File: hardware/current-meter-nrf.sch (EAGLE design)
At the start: 47 parts, among them IC1 TINY24/44/84-SSU, IC2 LM358, IC3 MAX1555, U2 NRF24L01SMD, U3 USB-MINIB-5PIN, X1 MC2, Y1 16M

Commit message: hw: cosmetic refactor
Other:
- note added: "Radio"
- note added: "nRF"
- note removed: "nRF Radio"
- moved on the sheet: BOX1, C10, C11, C12, C13, C14, C15, C16, C17, C18, C19, C3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

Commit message: hw: nrf: progress save
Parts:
- removed R1, R2: 68, rcl:R-EU_R0603
- removed R3: 1k5, rcl:R-EU_R0603
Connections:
- removed net N$1: R2.1, R3.1, U3.D-
- removed net N$2: R1.1, U3.D+
- removed net USB_DN: IC1.(PCINT9/XTAL2)PB1, R2.2
- removed net USB_DP: IC1.(PCINT10/INT0/OC0A/CKOUT)PB2, R1.2
- new net LED: IC1.(PCINT8/XTAL1/CLKI)PB0, LED1.A
- net A_EN: now also IC1.(PCINT9/XTAL2)PB1; no longer IC1.(PCINT8/XTAL1/CLKI)PB0, LED1.A
- net VCC: no longer R3.2
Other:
- moved on the sheet: IC3, ISP1, LED1, LED2, R10, R13, TP1, TP2

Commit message: hw: nrf: progress save
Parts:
- removed LED2: (no value), led:LEDSML0805
- removed R10: 330, rcl:R-EU_R0603
- added C1, C2: 1u, rcl:C-EUC0805
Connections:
- removed net N$20: LED2.C, R10.2
- net +5V: now also C2.1
- net CHG: now also IC1.(PCINT7/ICP/OC0B/ADC7)PA7; no longer R10.1
- net GND: now also C1.2, C2.2, LED1.C; no longer R13.1
- net LED: now also R13.2; no longer LED1.A
- net N$3: now also LED1.A, R13.1; no longer LED1.C, R13.2
- net RF_IRQ: now also IC1.(PCINT10/INT0/OC0A/CKOUT)PB2; no longer IC1.(PCINT7/ICP/OC0B/ADC7)PA7
- net VCC: now also C1.1; no longer LED2.A
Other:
- moved on the sheet: IC3, LED1, R13, TP1, TP2

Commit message: hw: nrf: progress save
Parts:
- TP1, TP2: value TPTP11R -> TPTP12R; device testpad:TPTP11R -> testpad:TPTP12R
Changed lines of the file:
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@@
 <grid distance="0.1" unitdist="inch" unit="inch" style="lines" multiple="1" display="no" altdistance="0.01" altunitdist="inch" altunit="inch"/>
 <layers>
-<layer number="1" name="Top" color="4" fill="1" visible="no" active="no"/>
-<layer number="16" name="Bottom" color="1" fill="1" visible="no" active="no"/>
-<layer number="17" name="Pads" color="2" fill="1" visible="no" active="no"/>
-<layer number="18" name="Vias" color="2" fill="1" visible="no" active="no"/>
-<layer number="19" name="Unrouted" color="6" fill="1" visible="no" active="no"/>
-<layer number="20" name="Dimension" color="15" fill="1" visible="no" active="no"/>
-<layer number="21" name="tPlace" color="7" fill="1" visible="no" active="no"/>
-<layer number="22" name="bPlace" color="7" fill="1" visible="no" active="no"/>
-<layer number="23" name="tOrigins" color="15" fill="1" visible="no" active="no"/>
-<layer number="24" name="bOrigins" color="15" fill="1" visible="no" active="no"/>
-<layer number="25" name="tNames" color="7" fill="1" visible="no" active="no"/>
-<layer number="26" name="bNames" color="7" fill="1" visible="no" active="no"/>
-<layer number="27" name="tValues" color="7" fill="1" visible="no" active="no"/>
-<layer number="28" name="bValues" color="7" fill="1" visible="no" active="no"/>
+<layer number="1" name="Top" color="4" fill="1" visible="yes" active="no"/>
+<layer number="16" name="Bottom" color="1" fill="1" visible="yes" active="no"/>
+<layer number="17" name="Pads" color="2" fill="1" visible="yes" active="no"/>
+<layer number="18" name="Vias" color="2" fill="1" visible="yes" active="no"/>
+<layer number="19" name="Unrouted" color="6" fill="1" visible="yes" active="no"/>
+<layer number="20" name="Dimension" color="15" fill="1" visible="yes" active="no"/>
+<layer number="21" name="tPlace" color="7" fill="1" visible="yes" active="no"/>
+<layer number="22" name="bPlace" color="7" fill="1" visible="yes" active="no"/>
+<layer number="23" name="tOrigins" color="15" fill="1" visible="yes" active="no"/>
+<layer number="24" name="bOrigins" color="15" fill="1" visible="yes" active="no"/>
+<layer number="25" name="tNames" color="7" fill="1" visible="yes" active="no"/>
+<layer number="26" name="bNames" color="7" fill="1" visible="yes" active="no"/>
+<layer number="27" name="tValues" color="7" fill="1" visible="yes" active="no"/>
+<layer number="28" name="bValues" color="7" fill="1" visible="yes" active="no"/>
 <layer number="29" name="tStop" color="7" fill="3" visible="no" active="no"/>
 <layer number="30" name="bStop" color="7" fill="6" visible="no" active="no"/>
@@
 <layer number="35" name="tGlue" color="7" fill="4" visible="no" active="no"/>
 <layer number="36" name="bGlue" color="7" fill="5" visible="no" active="no"/>
-<layer number="37" name="tTest" color="7" fill="1" visible="no" active="no"/>
-<layer number="38" name="bTest" color="7" fill="1" visible="no" active="no"/>
+<layer number="37" name="tTest" color="7" fill="1" visible="yes" active="no"/>
+<layer number="38" name="bTest" color="7" fill="1" visible="yes" active="no"/>
 <layer number="39" name="tKeepout" color="4" fill="11" visible="no" active="no"/>
 <layer number="40" name="bKeepout" color="1" fill="11" visible="no" active="no"/>
@@
 <layer number="44" name="Drills" color="7" fill="1" visible="no" active="no"/>
 <layer number="45" name="Holes" color="7" fill="1" visible="no" active="no"/>
-<layer number="46" name="Milling" color="3" fill="1" visible="no" active="no"/>
-<layer number="47" name="Measures" color="7" fill="1" visible="no" active="no"/>
-<layer number="48" name="Document" color="7" fill="1" visible="no" active="no"/>
-<layer number="49" name="Reference" color="7" fill="1" visible="no" active="no"/>
-<layer number="50" name="dxf" color="7" fill="1" visible="no" active="no"/>
-<layer number="51" name="tDocu" color="7" fill="1" visible="no" active="no"/>
-<layer number="52" name="bDocu" color="7" fill="1" visible="no" active="no"/>
-<layer number="53" name="tGND_GNDA" color="7" fill="9" visible="no" active="no"/>
-<layer number="54" name="bGND_GNDA" color="1" fill="9" visible="no" active="no"/>
-<layer number="56" name="wert" color="7" fill="1" visible="no" active="no"/>
+<layer number="46" name="Milling" color="3" fill="1" visible="yes" active="no"/>
+<layer number="47" name="Measures" color="7" fill="1" visible="yes" active="no"/>
+<layer number="48" name="Document" color="7" fill="1" visible="yes" active="no"/>
+<layer number="49" name="Reference" color="7" fill="1" visible="yes" active="no"/>
+<layer number="50" name="dxf" color="7" fill="1" visible="yes" active="no"/>
+<layer number="51" name="tDocu" color="7" fill="1" visible="yes" active="no"/>
+<layer number="52" name="bDocu" color="7" fill="1" visible="yes" active="no"/>
+<layer number="53" name="tGND_GNDA" color="7" fill="9" visible="yes" active="no"/>
+<layer number="54" name="bGND_GNDA" color="1" fill="9" visible="yes" active="no"/>
+<layer number="56" name="wert" color="7" fill="1" visible="yes" active="no"/>
 <layer number="91" name="Nets" color="2" fill="1" visible="yes" active="yes"/>
 <layer number="92" name="Busses" color="1" fill="1" visible="yes" active="yes"/>
@@
 <part name="IC3" library="maxim" deviceset="MAX1555" device=""/>
 <part name="GND27" library="supply1" deviceset="GND" device=""/>
-<part name="TP1" library="testpad" deviceset="TP" device="TP11R"/>
-<part name="TP2" library="testpad" deviceset="TP" device="TP11R"/>
+<part name="TP1" library="testpad" deviceset="TP" device="TP12R"/>
+<part name="TP2" library="testpad" deviceset="TP" device="TP12R"/>
 <part name="U3" library="SparkFun" deviceset="USB-MINIB" device="-5PIN"/>
 <part name="GND17" library="supply1" deviceset="GND" device=""/>

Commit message: nrf: hw: progress save
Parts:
- added C4: .1u, rcl:C-EUC0805
- added U4: V_REG_LDOSMD, SparkFun-PowerIC:V_REG_LDOSMD
- C1, C2: value 1u -> .1u
- C3: value 100n -> .1u
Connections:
- new net VBATT: C4.1, IC3.BAT, TP1.TP, U4.EN, U4.IN
- net GND: now also C4.2, U4.GND
- net VCC: now also U4.OUT; no longer IC3.BAT, TP1.TP
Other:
- note added: "LDO"
- moved on the sheet: BOX1, C1, C11, C12, C13, C14, C15, C16, C17, C18, C19, C2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

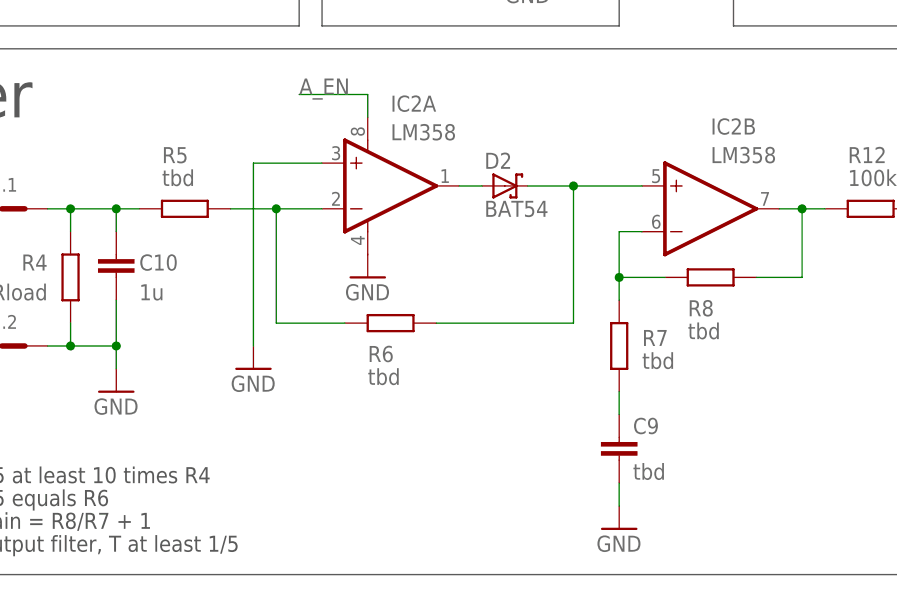
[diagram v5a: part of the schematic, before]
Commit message: hw: nrf: add missing part value
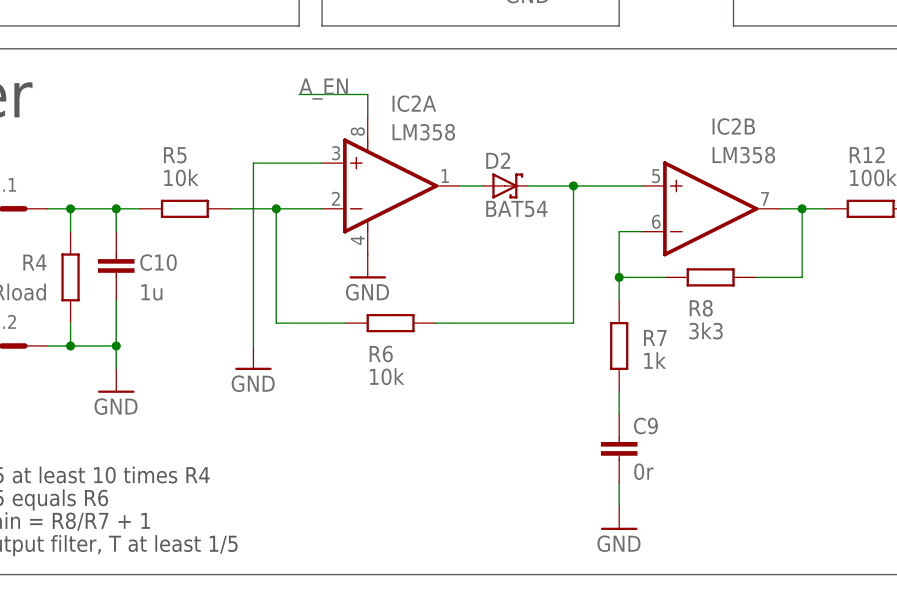
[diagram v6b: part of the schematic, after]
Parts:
- C9: value tbd -> 0r
- R5, R6: value tbd -> 10k
- R7: value tbd -> 1k
- R8: value tbd -> 3k3
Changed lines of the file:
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@@
 <part name="GND5" library="supply1" deviceset="GND" device=""/>
 <part name="R4" library="rcl" deviceset="R-EU_" device="R0805" value="Rload"/>
-<part name="R5" library="rcl" deviceset="R-EU_" device="R0603" value="tbd"/>
-<part name="R6" library="rcl" deviceset="R-EU_" device="R0603" value="tbd"/>
+<part name="R5" library="rcl" deviceset="R-EU_" device="R0603" value="10k"/>
+<part name="R6" library="rcl" deviceset="R-EU_" device="R0603" value="10k"/>
 <part name="GND6" library="supply1" deviceset="GND" device=""/>
-<part name="R7" library="rcl" deviceset="R-EU_" device="R0603" value="tbd"/>
-<part name="R8" library="rcl" deviceset="R-EU_" device="R0603" value="tbd"/>
+<part name="R7" library="rcl" deviceset="R-EU_" device="R0603" value="1k"/>
+<part name="R8" library="rcl" deviceset="R-EU_" device="R0603" value="3k3"/>
 <part name="GND8" library="supply1" deviceset="GND" device=""/>
 <part name="GND9" library="supply1" deviceset="GND" device=""/>
@@
 <part name="GND16" library="supply1" deviceset="GND" device=""/>
 <part name="LICENSE1" library="balto" deviceset="CC_BY-SA" device="" value="Fabio Baltieri"/>
-<part name="C9" library="rcl" deviceset="C-EU" device="C0805" value="tbd"/>
+<part name="C9" library="rcl" deviceset="C-EU" device="C0805" value="0r"/>
 <part name="C10" library="rcl" deviceset="C-EU" device="C0805" value="1u"/>
 <part name="C11" library="rcl" deviceset="C-EU" device="C0603" value="1p5"/>
